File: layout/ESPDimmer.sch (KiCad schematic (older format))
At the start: 11 parts, among them P1 CONN_01X03, P2 Serial, P3 LED, P4 ProgMod, Q1 IRLB8721, U1 TLV1117, U2 ESP-12E

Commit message: Updated schematic and PCB, initial firmware (no wifi, only encoder control)
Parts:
- removed P1: CONN_01X03, Connect:BARREL_JACK, symbol CONN_01X03
- removed P4: ProgMod, Socket_Strips:Socket_Strip_Straight_1x02, symbol CONN_01X02
- removed Q1: IRLB8721, TO_SOT_Packages_THT:TO-220_Neutral123_Vertical, symbol Q_NMOS_GDS
- removed R1: 10k, Resistors_SMD:R_0805, symbol R_Small
- removed U1: TLV1117, TO_SOT_Packages_SMD:SOT-223, symbol TLV1117
- removed U2: ESP-12E, ESP8266:ESP-12E, symbol ESP-12E
- added C4, C5, C6: 100n, Capacitor_SMD:C_0805_2012Metric_Pad1.18x1.45mm_HandSolder, symbol Device:C
- added P1: IN, Connector_PinHeader_2.54mm:PinHeader_1x02_P2.54mm_Vertical, symbol ESPDimmer-rescue:CONN_01X02
- added Q1: IRLZ44N, Package_TO_SOT_THT:TO-220-3_Horizontal_TabDown, symbol Transistor_FET:IRLZ44N
- added R1, R2, R3: 10k, Resistor_SMD:R_0805_2012Metric_Pad1.20x1.40mm_HandSolder, symbol Device:R
- added R4, R5, R6: 1k, Resistor_SMD:R_0805_2012Metric_Pad1.20x1.40mm_HandSolder, symbol Device:R
- added SW1: Rotary_Encoder_Switch, Rotary_Encoder:RotaryEncoder_Alps_EC11E-Switch_Vertical_H20mm_CircularMountingHoles, symbol Device:Rotary_Encoder_Switch
- added U1: AMS1117-3.3, Package_TO_SOT_SMD:SOT-223-3_TabPin2, symbol Regulator_Linear:AMS1117-3.3
- added U2: ESP-12E, ESP8266:ESP-12E_SMD_CHI, symbol RF_Module:ESP-12E
- added U3: 74HC14, Package_SO:SOIC-14_3.9x8.7mm_P1.27mm, symbol 74xx:74HC14
- C1, C2, C3: footprint Capacitors_SMD:C_0402 -> Capacitor_SMD:C_0805_2012Metric_Pad1.18x1.45mm_HandSolder; symbol C_Small -> Device:C_Small
- P2: footprint Socket_Strips:Socket_Strip_Straight_1x03 -> Connector_PinHeader_2.54mm:PinHeader_1x03_P2.54mm_Vertical; symbol CONN_01X03 -> ESPDimmer-rescue:CONN_01X03
- P3: value LED -> OUT; footprint Connect:AK300-2 -> Connector_PinHeader_2.54mm:PinHeader_1x02_P2.54mm_Vertical; symbol CONN_01X02 -> ESPDimmer-rescue:CONN_01X02
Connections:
- net labels removed: GPIO0, RX, TX
- wire segments 43 -> 76
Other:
- moved on the sheet: P2, P3

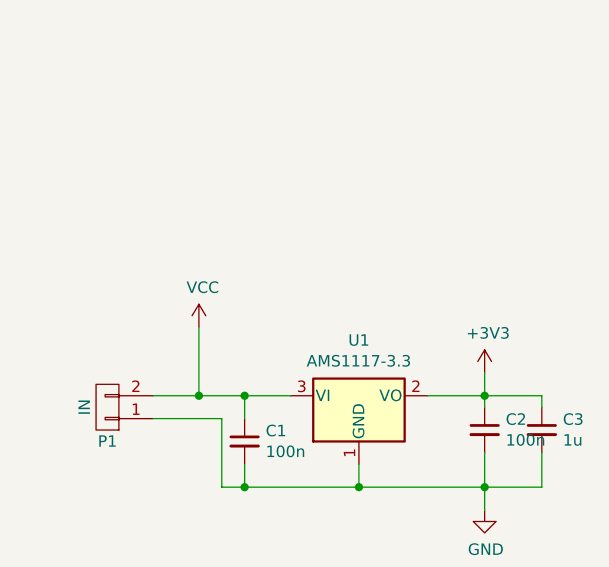
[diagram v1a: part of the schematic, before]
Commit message: Added NTP and basic web UI
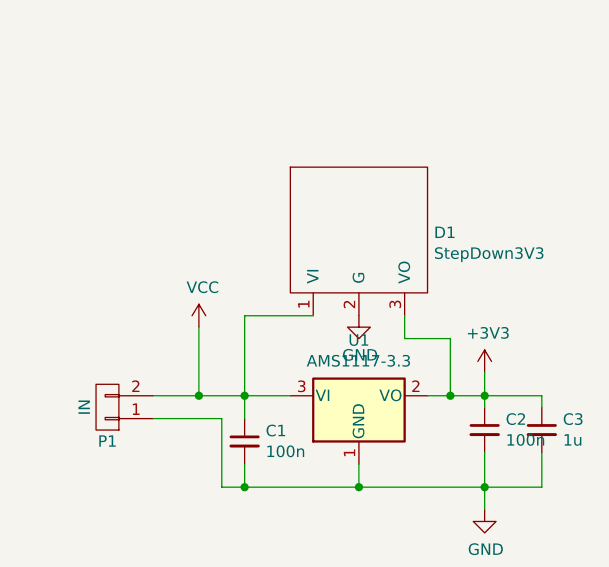
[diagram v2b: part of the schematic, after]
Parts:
- added D1: StepDown3V3, Package_TO_SOT_THT:TO-220-3_Vertical, symbol MY:StepDown3V3
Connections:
- net +3V3: now also D1.3 (VO)
- net GND: now also D1.2 (G)
- net VCC: now also D1.1 (VI)
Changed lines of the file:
@@
 Wire Wire Line
 	10350 5950 10600 5950
-Wire Wire Line
-	9100 5550 9300 5550
 $Comp
 L Device:Rotary_Encoder_Switch SW1
@@
 Connection ~ 9300 5550
 Wire Wire Line
-	10100 5550 10350 5550
+	10100 5550 10200 5550
 Wire Wire Line
 	9800 5850 9800 5950
@@
 Wire Wire Line
 	6400 4900 6400 5650
+$Comp
+L MY:StepDown3V3 D1
+U 1 1 62742F5D
+P 9800 4700
+F 0 "D1" H 10128 4563 50  0000 L CNN
+F 1 "StepDown3V3" H 10128 4472 50  0000 L CNN
+F 2 "Package_TO_SOT_THT:TO-220-3_Vertical" H 9800 4700 50  0001 C CNN
+F 3 "" H 9800 4700 50  0001 C CNN
+	1    9800 4700
+	1    0    0    -1
+$EndComp
+Wire Wire Line
+	9100 5550 9300 5550
+Wire Wire Line
+	9600 5200 9300 5200
+Wire Wire Line
+	9300 5200 9300 5550
+Wire Wire Line
+	10000 5200 10000 5300
+Wire Wire Line
+	10000 5300 10200 5300
+Wire Wire Line
+	10200 5300 10200 5550
+Connection ~ 10200 5550
+Wire Wire Line
+	10200 5550 10350 5550
+$Comp
+L power:GND #PWR0108
+U 1 1 62749E26
+P 9800 5200
+F 0 "#PWR0108" H 9800 4950 50  0001 C CNN
+F 1 "GND" H 9805 5027 50  0000 C CNN
+F 2 "" H 9800 5200 50  0000 C CNN
+F 3 "" H 9800 5200 50  0000 C CNN
+	1    9800 5200
+	1    0    0    -1
+$EndComp
 $EndSCHEMATC
